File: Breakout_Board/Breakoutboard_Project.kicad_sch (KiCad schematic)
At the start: 1 part, among them U1 ADXL380-2BCCZ-RL7

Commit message: Added costum footprint
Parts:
- added U2: STM32F411CCUx, Package_DFN_QFN:QFN-48-1EP_7x7mm_P0.5mm_EP5.6x5.6mm, symbol MCU_ST_STM32F4:STM32F411CCUx
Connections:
- new net: U2.23 (VSS), U2.35 (VSS), U2.47 (VSS), U2.49 (VSS)
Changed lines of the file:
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@@
+		)
+	)
+	(symbol
+		(lib_id "MCU_ST_STM32F4:STM32F411CCUx")
+		(at 179.07 90.17 0)
+		(unit 1)
+		(body_style 1)
+		(exclude_from_sim no)
+		(in_bom yes)
+		(on_board yes)
+		(in_pos_files yes)
+		(dnp no)
+		(fields_autoplaced yes)
+		(property "Reference" "U2"
+			(at 183.7533 130.81 0)
+			(show_name no)
+			(do_not_autoplace no)
+			(effects
+				(font
+					(size 1.27 1.27)
+				)
+				(justify left)
+			)
+		)
+		(property "Value" "STM32F411CCUx"
+			(at 183.7533 133.35 0)
+			(show_name no)
+			(do_not_autoplace no)
+			(effects
+				(font
+					(size 1.27 1.27)
+				)
+				(justify left)
+			)
+		)
+		(property "Footprint" "Package_DFN_QFN:QFN-48-1EP_7x7mm_P0.5mm_EP5.6x5.6mm"
+			(at 163.83 128.27 0)
+			(hide yes)
+			(show_name no)
+			(do_not_autoplace no)
+			(effects
+				(font
+					(size 1.27 1.27)
+				)
+				(justify right)
+			)
+		)
+		(property "Datasheet" "https://www.st.com/resource/en/datasheet/stm32f411cc.pdf"
+			(at 179.07 90.17 0)
+			(hide yes)
+			(show_name no)
+			(do_not_autoplace no)
+			(effects
+				(font
+					(size 1.27 1.27)
+				)
+			)
+		)
+		(property "Description" "STMicroelectronics Arm Cortex-M4 MCU, 256KB flash, 128KB RAM, 100 MHz, 1.7-3.6V, 36 GPIO, UFQFPN48"
+			(at 179.07 90.17 0)
+			(hide yes)
+			(show_name no)
+			(do_not_autoplace no)
+			(effects
+				(font
+					(size 1.27 1.27)
+				)
+			)
+		)
+		(pin "25"
+		)
+		(pin "10"
+		)
+		(pin "18"
+		)
+		(pin "6"
+		)
+		(pin "13"
+		)
+		(pin "1"
+		)
+		(pin "26"
+		)
+		(pin "14"
+		)
+		(pin "5"
+		)
+		(pin "21"
+		)
+		(pin "2"
+		)
+		(pin "15"
+		)
+		(pin "23"
+		)
+		(pin "27"
+		)
+		(pin "17"
+		)
+		(pin "19"
+		)
+		(pin "16"
+		)
+		(pin "24"
+		)
+		(pin "12"
+		)
+		(pin "20"
+		)
+		(pin "7"
+		)
+		(pin "3"
+		)
+		(pin "22"
+		)
+		(pin "8"
+		)
+		(pin "4"
+		)
+		(pin "9"
+		)
+		(pin "11"
+		)
+		(pin "46"
+		)
+		(pin "32"
+		)
+		(pin "45"
+		)
+		(pin "43"
+		)
+		(pin "40"
+		)
+		(pin "41"
+		)
+		(pin "33"
+		)
+		(pin "30"
+		)
+		(pin "44"
+		)
+		(pin "48"
+		)
+		(pin "36"
+		)
+		(pin "39"
+		)
+		(pin "31"
+		)
+		(pin "38"
+		)
+		(pin "28"
+		)
+		(pin "42"
+		)
+		(pin "49"
+		)
+		(pin "29"
+		)
+		(pin "37"
+		)
+		(pin "35"
+		)
+		(pin "34"
+		)
+		(pin "47"
+		)
+		(instances
+			(project "Breakoutboard_Project"
+				(path "/e5b5f554-bb6f-4ecb-9cfb-c4d676c83727"
+					(reference "U2")
+					(unit 1)
+				)
+			)
 		)
 	)

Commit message: added the costum things to main pcb and sch
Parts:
- removed U2: STM32F411CCUx, Package_DFN_QFN:QFN-48-1EP_7x7mm_P0.5mm_EP5.6x5.6mm, symbol MCU_ST_STM32F4:STM32F411CCUx
- added U2: (no value), SeniorDesignLibrary:BlackpillGeneric, symbol SeniorDesignLibrary:STM32F411_
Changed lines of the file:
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@@
 	)
 	(symbol
-		(lib_id "MCU_ST_STM32F4:STM32F411CCUx")
-		(at 179.07 90.17 0)
+		(lib_id "SeniorDesignLibrary:STM32F411_")
+		(at 57.15 87.63 0)
 		(unit 1)
 		(body_style 1)
@@
 		(fields_autoplaced yes)
 		(property "Reference" "U2"
-			(at 183.7533 130.81 0)
+			(at 58.0233 118.11 0)
 			(show_name no)
 			(do_not_autoplace no)
@@
 			)
 		)
-		(property "Value" "STM32F411CCUx"
-			(at 183.7533 133.35 0)
+		(property "Value" ""
+			(at 57.15 87.63 0)
 			(show_name no)
 			(do_not_autoplace no)
@@
 					(size 1.27 1.27)
 				)
-				(justify left)
 			)
 		)
-		(property "Footprint" "Package_DFN_QFN:QFN-48-1EP_7x7mm_P0.5mm_EP5.6x5.6mm"
-			(at 163.83 128.27 0)
-			(hide yes)
-			(show_name no)
-			(do_not_autoplace no)
-			(effects
-				(font
-					(size 1.27 1.27)
-				)
-				(justify right)
-			)
-		)
-		(property "Datasheet" "https://www.st.com/resource/en/datasheet/stm32f411cc.pdf"
-			(at 179.07 90.17 0)
+		(property "Footprint" "SeniorDesignLibrary:BlackpillGeneric"
+			(at 57.15 87.63 0)
 			(hide yes)
 			(show_name no)
@@
 			)
 		)
-		(property "Description" "STMicroelectronics Arm Cortex-M4 MCU, 256KB flash, 128KB RAM, 100 MHz, 1.7-3.6V, 36 GPIO, UFQFPN48"
-			(at 179.07 90.17 0)
+		(property "Datasheet" ""
+			(at 57.15 87.63 0)
 			(hide yes)
 			(show_name no)
@@
 			)
 		)
-		(pin "25"
+		(property "Description" ""
+			(at 57.15 87.63 0)
+			(hide yes)
+			(show_name no)
+			(do_not_autoplace no)
+			(effects
+				(font
+					(size 1.27 1.27)
+				)
+			)
+		)
+		(pin "20"
+		)
+		(pin "15"
+		)
+		(pin "7"
 		)
 		(pin "10"
 		)
-		(pin "18"
-		)
-		(pin "6"
-		)
-		(pin "13"
-		)
-		(pin "1"
-		)
-		(pin "26"
-		)
-		(pin "14"
-		)
-		(pin "5"
-		)
-		(pin "21"
+		(pin "17"
 		)
 		(pin "2"
 		)
-		(pin "15"
-		)
-		(pin "23"
-		)
-		(pin "27"
-		)
-		(pin "17"
-		)
-		(pin "19"
-		)
 		(pin "16"
-		)
-		(pin "24"
-		)
-		(pin "12"
-		)
-		(pin "20"
-		)
-		(pin "7"
 		)
 		(pin "3"
@@
 		(pin "22"
 		)
-		(pin "8"
+		(pin "14"
+		)
+		(pin "9"
+		)
+		(pin "1"
+		)
+		(pin "21"
+		)
+		(pin "11"
+		)
+		(pin "12"
 		)
 		(pin "4"
 		)
-		(pin "9"
+		(pin "8"
 		)
-		(pin "11"
+		(pin "19"
 		)
-		(pin "46"
+		(pin "23"
+		)
+		(pin "18"
+		)
+		(pin "13"
+		)
+		(pin "6"
+		)
+		(pin "5"
+		)
+		(pin "30"
+		)
+		(pin "35"
+		)
+		(pin "28"
+		)
+		(pin "27"
 		)
 		(pin "32"
 		)
-		(pin "45"
+		(pin "24"
 		)
-		(pin "43"
+		(pin "26"
+		)
+		(pin "33"
+		)
+		(pin "31"
+		)
+		(pin "34"
+		)
+		(pin "25"
+		)
+		(pin "29"
+		)
+		(pin "38"
+		)
+		(pin "36"
+		)
+		(pin "37"
+		)
+		(pin "39"
 		)
 		(pin "40"
 		)
-		(pin "41"
-		)
-		(pin "33"
-		)
-		(pin "30"
-		)
-		(pin "44"
-		)
-		(pin "48"
-		)
-		(pin "36"
-		)
-		(pin "39"
-		)
-		(pin "31"
-		)
-		(pin "38"
-		)
-		(pin "28"
-		)
-		(pin "42"
-		)
-		(pin "49"
-		)
-		(pin "29"
-		)
-		(pin "37"
-		)
-		(pin "35"
-		)
-		(pin "34"
-		)
-		(pin "47"
-		)
 		(instances

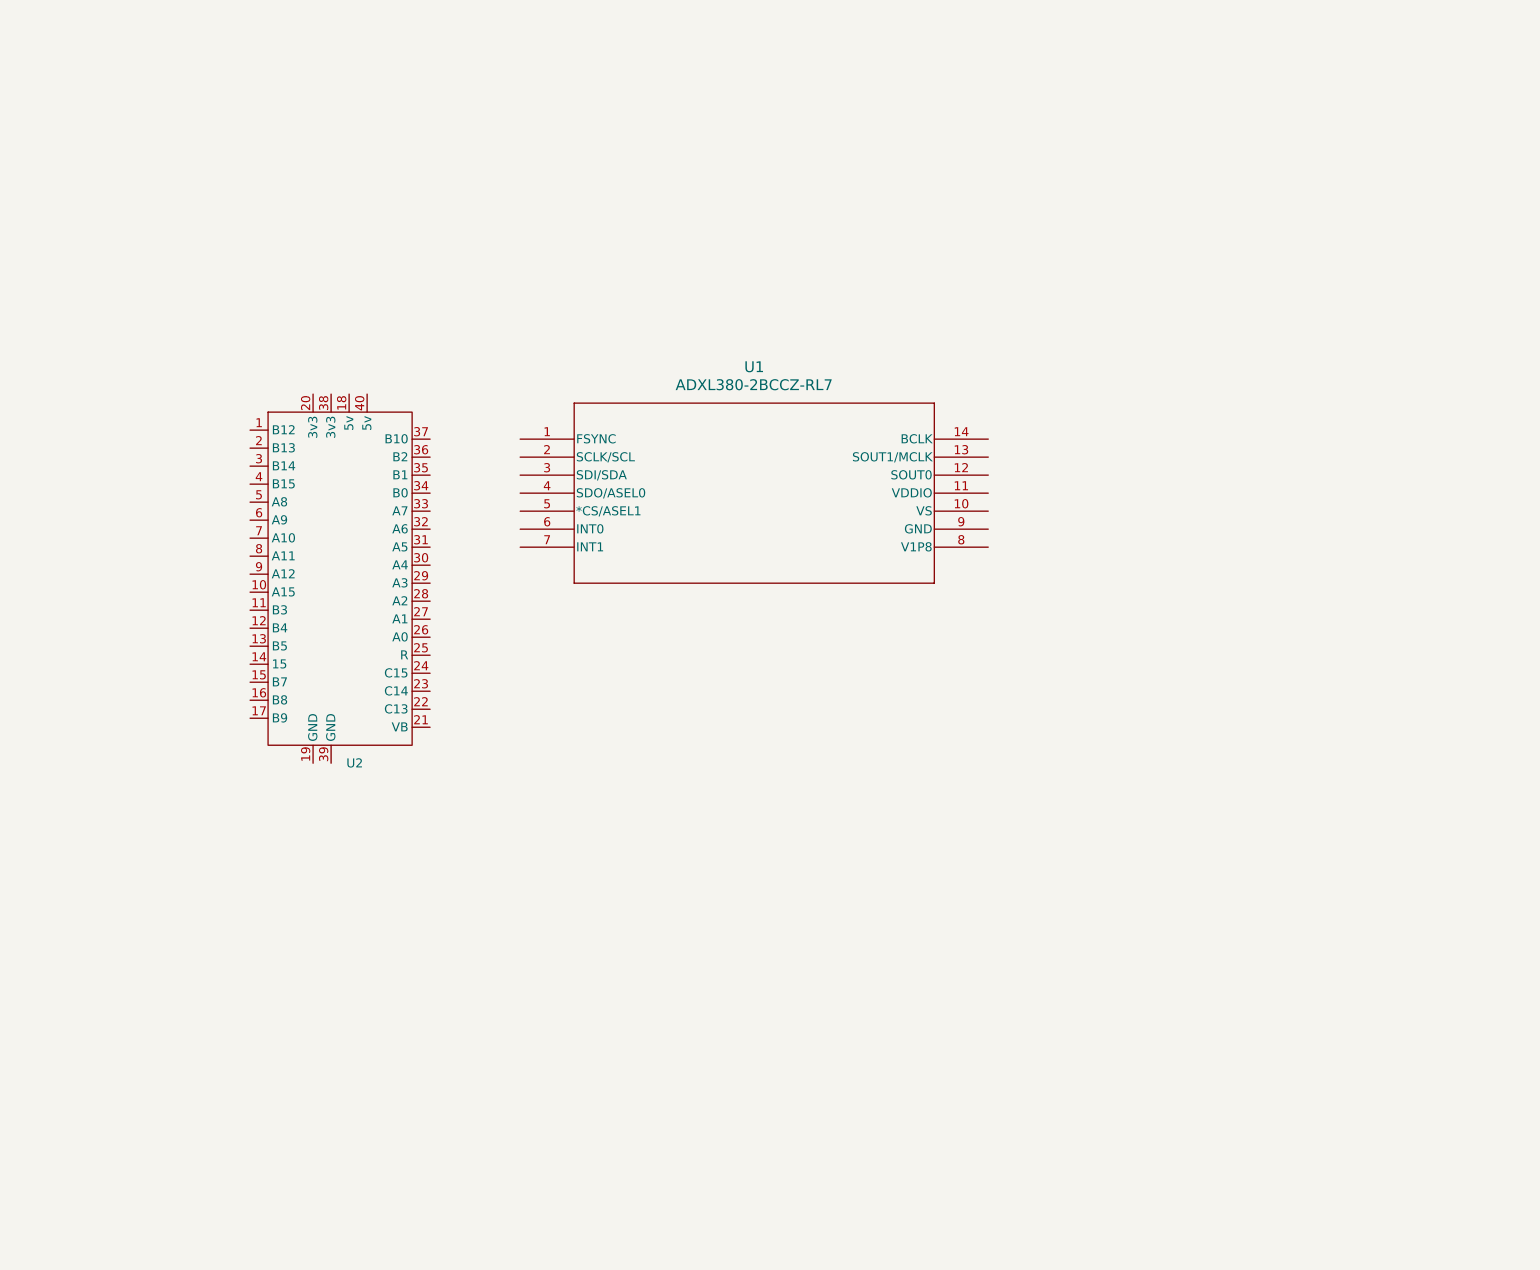
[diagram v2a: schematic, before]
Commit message: added more organization
heriarchical sheets yay, added all the compoennts we will be working with and seperated into sheets so we can work on the in parralel easier.
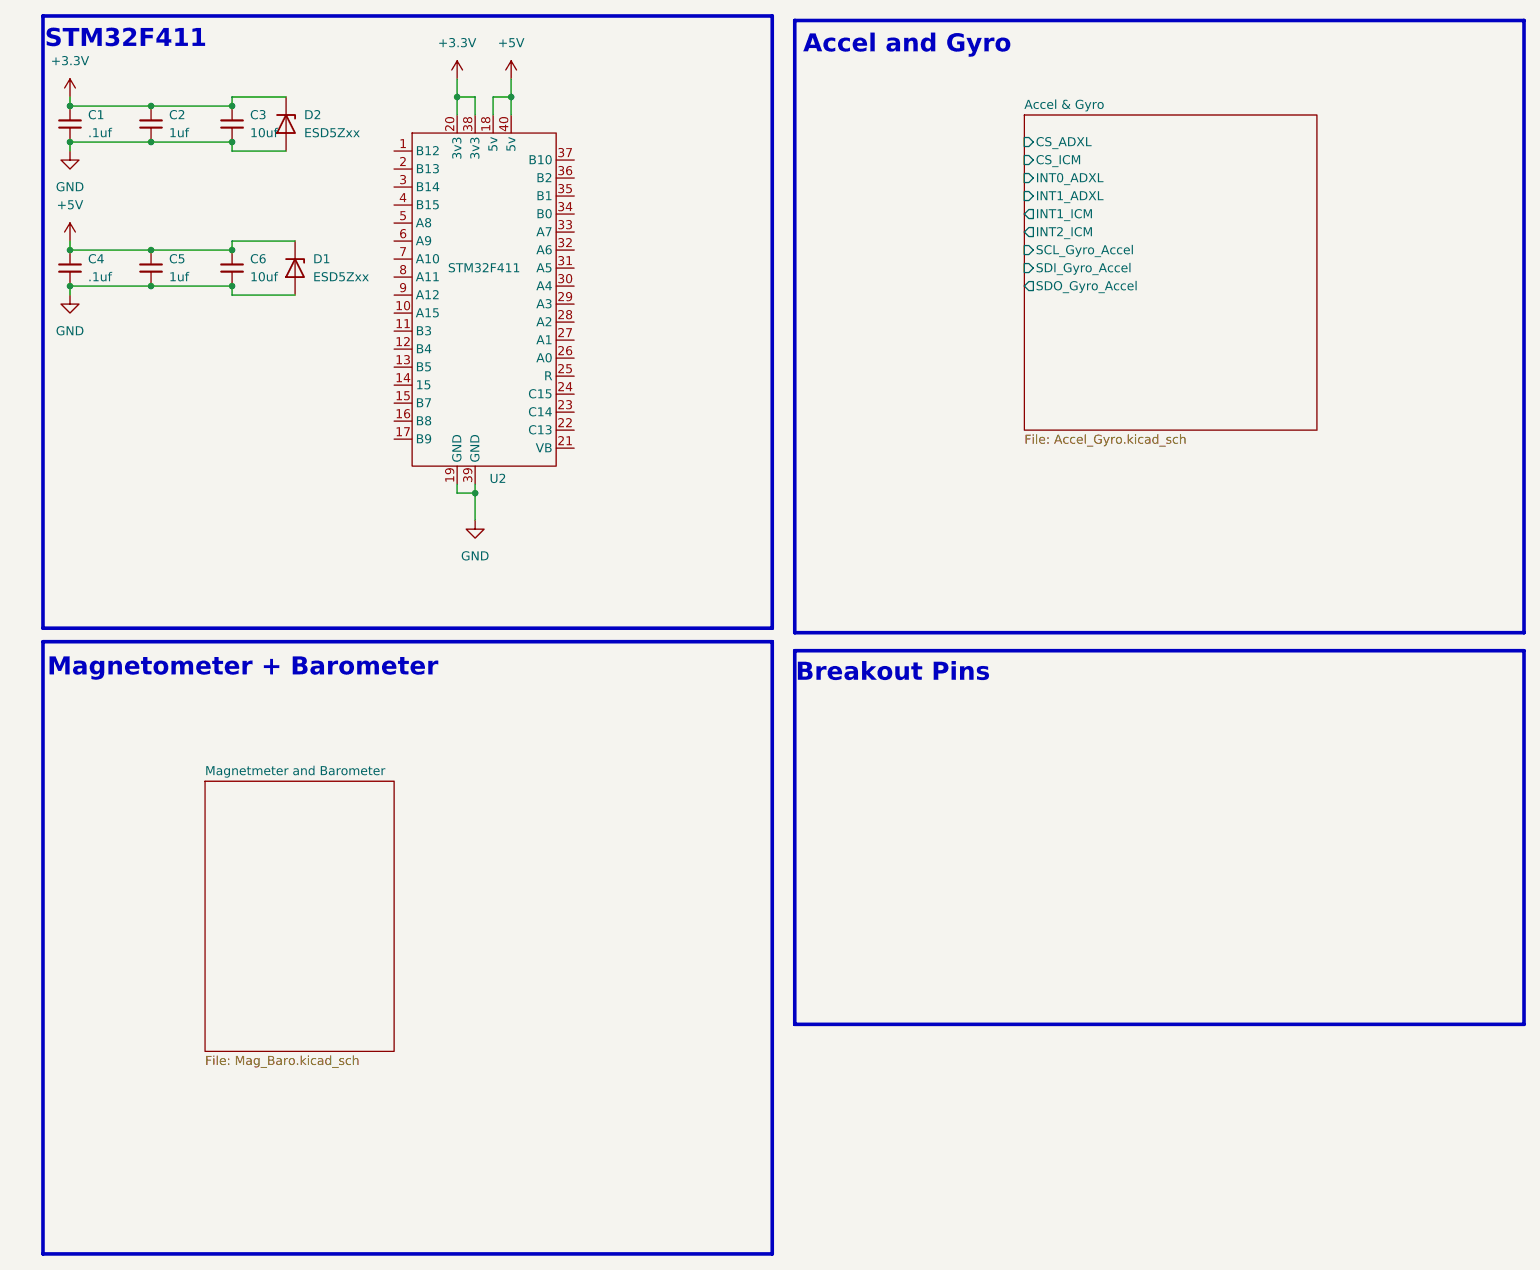
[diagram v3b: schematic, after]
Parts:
- removed U1: ADXL380-2BCCZ-RL7, CC-14-3_ADI, symbol ADXL380:ADXL380-2BCCZ-RL7
- added C1, C4: .1uf, Capacitor_SMD:C_0805_2012Metric_Pad1.18x1.45mm_HandSolder, symbol Device:C_Small
- added C2, C5: 1uf, Capacitor_SMD:C_0805_2012Metric_Pad1.18x1.45mm_HandSolder, symbol Device:C_Small
- added C3, C6: 10uf, Capacitor_SMD:C_0805_2012Metric_Pad1.18x1.45mm_HandSolder, symbol Device:C_Small
- added D1, D2: ESD5Zxx, Diode_SMD:D_SOD-523, symbol Diode:ESD5Zxx
- U2: value (none) -> STM32F411
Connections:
- net +5V: now reaches U2.18 (5v)
- net +5V: now also U2.40 (5v), C4.1, C5.1, C6.1, D1.1 (K)
- net GND: now reaches U2.19 (GND)
- net GND: now also U2.39 (GND), C1.2, C2.2, C3.2, C4.2, C5.2, C6.2, D1.2 (A), D2.2 (A)
- net +3.3V: now reaches U2.20 (3v3)
- net +3.3V: now also U2.38 (3v3), C1.1, C2.1, C3.1, D2.1 (K)
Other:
- added sheet Accel & Gyro (Accel_Gyro.kicad_sch)
- added sheet Magnetmeter and Barometer (Mag_Baro.kicad_sch)
- note added: "Accel and Gyro"
- note added: "Breakout Pins"
- note added: "Magnetometer + Barometer"
- note added: "STM32F411"
- moved on the sheet: U2

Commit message: mmm more stuff
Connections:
- net CS_ADXL: now reaches U2.29 (A3)
- net CS_ICM: now reaches U2.30 (A4)
- net SCLK_Accel_gyro: now reaches U2.31 (A5)
- net MISO_Accel_gyro: now reaches U2.32 (A6)
- net MOSI_Accel_gyro: now reaches U2.33 (A7)
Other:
- added sheet Breakouts (Breakouts.kicad_sch)
- sheet Accel & Gyro ports: added FSYNC_ADXL, FSYNC_ICM; removed INT2_ICM
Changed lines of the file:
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@@
 	(wire
 		(pts
+			(xy 90.17 45.72) (xy 92.71 45.72)
+		)
+		(stroke
+			(width 0)
+			(type default)
+		)
+	)
+	(wire
+		(pts
 			(xy 76.2 80.01) (xy 76.2 83.82)
 		)
@@
 	(wire
 		(pts
+			(xy 149.86 43.18) (xy 153.67 43.18)
+		)
+		(stroke
+			(width 0)
+			(type default)
+		)
+	)
+	(wire
+		(pts
 			(xy 41.91 50.8) (xy 41.91 52.07)
 		)
@@
 	(wire
 		(pts
+			(xy 90.17 48.26) (xy 92.71 48.26)
+		)
+		(stroke
+			(width 0)
+			(type default)
+		)
+	)
+	(wire
+		(pts
+			(xy 149.86 30.48) (xy 153.67 30.48)
+		)
+		(stroke
+			(width 0)
+			(type default)
+		)
+	)
+	(wire
+		(pts
 			(xy 30.48 25.4) (xy 41.91 25.4)
 		)
@@
 	(wire
 		(pts
+			(xy 93.98 53.34) (xy 90.17 53.34)
+		)
+		(stroke
+			(width 0)
+			(type default)
+		)
+	)
+	(wire
+		(pts
 			(xy 19.05 50.8) (xy 30.48 50.8)
 		)
@@
 	(wire
 		(pts
+			(xy 93.98 50.8) (xy 90.17 50.8)
+		)
+		(stroke
+			(width 0)
+			(type default)
+		)
+	)
+	(wire
+		(pts
+			(xy 149.86 33.02) (xy 153.67 33.02)
+		)
+		(stroke
+			(width 0)
+			(type default)
+		)
+	)
+	(wire
+		(pts
+			(xy 149.86 45.72) (xy 153.67 45.72)
+		)
+		(stroke
+			(width 0)
+			(type default)
+		)
+	)
+	(wire
+		(pts
 			(xy 41.91 31.75) (xy 49.53 31.75)
 		)
@@
 	(wire
 		(pts
+			(xy 149.86 48.26) (xy 153.67 48.26)
+		)
+		(stroke
+			(width 0)
+			(type default)
+		)
+	)
+	(wire
+		(pts
+			(xy 90.17 43.18) (xy 92.71 43.18)
+		)
+		(stroke
+			(width 0)
+			(type default)
+		)
+	)
+	(wire
+		(pts
 			(xy 41.91 52.07) (xy 50.8 52.07)
 		)
@@
 		)
 	)
+	(label "MOSI_Accel_gyro"
+		(at 92.71 43.18 0)
+		(effects
+			(font
+				(size 1.27 1.27)
+			)
+			(justify left bottom)
+		)
+	)
+	(label "MOSI_Accel_gyro"
+		(at 149.86 45.72 180)
+		(effects
+			(font
+				(size 1.27 1.27)
+			)
+			(justify right bottom)
+		)
+	)
+	(label "CS_ADXL"
+		(at 93.98 53.34 0)
+		(effects
+			(font
+				(size 1.27 1.27)
+			)
+			(justify left bottom)
+		)
+	)
+	(label "MISO_Accel_gyro"
+		(at 149.86 48.26 180)
+		(effects
+			(font
+				(size 1.27 1.27)
+			)
+			(justify right bottom)
+		)
+	)
+	(label "SCLK_Accel_gyro"
+		(at 92.71 48.26 0)
+		(effects
+			(font
+				(size 1.27 1.27)
+			)
+			(justify left bottom)
+		)
+	)
+	(label "MISO_Accel_gyro"
+		(at 92.71 45.72 0)
+		(effects
+			(font
+				(size 1.27 1.27)
+			)
+			(justify left bottom)
+		)
+	)
+	(label "CS_ICM"
+		(at 149.86 33.02 180)
+		(effects
+			(font
+				(size 1.27 1.27)
+			)
+			(justify right bottom)
+		)
+	)
+	(label "SCLK_Accel_gyro"
+		(at 149.86 43.18 180)
+		(effects
+			(font
+				(size 1.27 1.27)
+			)
+			(justify right bottom)
+		)
+	)
+	(label "CS_ICM"
+		(at 93.98 50.8 0)
+		(effects
+			(font
+				(size 1.27 1.27)
+			)
+			(justify left bottom)
+		)
+	)
+	(label "CS_ADXL"
+		(at 149.86 30.48 180)
+		(effects
+			(font
+				(size 1.27 1.27)
+			)
+			(justify right bottom)
+		)
+	)
 	(symbol
 		(lib_id "power:GND")
@@
 			)
 		)
-		(pin "INT2_ICM" output
+		(pin "SCL_Gyro_Accel" input
 			(at 153.67 43.18 180)
 			(effects
@@
 			)
 		)
-		(pin "SCL_Gyro_Accel" input
+		(pin "SDI_Gyro_Accel" input
 			(at 153.67 45.72 180)
 			(effects
@@
 			)
 		)
-		(pin "SDI_Gyro_Accel" input
+		(pin "SDO_Gyro_Accel" output
 			(at 153.67 48.26 180)
 			(effects
@@
 			)
 		)
-		(pin "SDO_Gyro_Accel" output
+		(pin "FSYNC_ADXL" input
 			(at 153.67 50.8 180)
 			(effects
@@
 			)
 		)
+		(pin "FSYNC_ICM" input
+			(at 153.67 53.34 180)
+			(effects
+				(font
+					(size 1.27 1.27)
+				)
+				(justify left)
+			)
+		)
 		(instances
 			(project "Breakoutboard_Project"
@@
 				)
 			)
+		)
+	)
+	(sheet
+		(at 128.905 115.57)
+		(size 41.275 23.495)
+		(exclude_from_sim no)
+		(in_bom yes)
+		(on_board yes)
+		(dnp no)
+		(fields_autoplaced yes)
+		(stroke
+			(width 0.1524)
+			(type solid)
+		)
+		(fill
+			(color 0 0 0 0)
+		)
+		(property "Sheetname" "Breakouts"
+			(at 128.905 114.8584 0)
+			(show_name no)
+			(do_not_autoplace no)
+			(effects
+				(font
+					(size 1.27 1.27)
+				)
+				(justify left bottom)
+			)
+		)
+		(property "Sheetfile" "Breakouts.kicad_sch"
+			(at 128.905 139.6496 0)
+			(show_name no)
+			(do_not_autoplace no)
+			(effects
+				(font
+					(size 1.27 1.27)
+				)
+				(justify left top)
+			)
+		)
+		(instances
+			(project "Breakoutboard_Project"
+				(path "/e5b5f554-bb6f-4ecb-9cfb-c4d676c83727"
+					(page "4")
+				)
+			)
